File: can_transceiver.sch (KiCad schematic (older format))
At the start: 9 parts

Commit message: Add vias and ground connections
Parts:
- gave numbers to parts that had none: 9
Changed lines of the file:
@@
 $EndDescr
 $Comp
-L SN65HVD256 U?
+L SN65HVD256 U201
 U 1 1 5A128E97
 P 6320 3680
-F 0 "U?" H 6320 3680 60  0000 C CNN
+F 0 "U201" H 6320 3680 60  0000 C CNN
 F 1 "SN65HVD256" H 6320 4080 60  0000 C CNN
 F 2 "breakout:TI_SOIC8" H 6320 3680 60  0001 C CNN
@@
 $EndComp
 $Comp
-L R_Small R?
+L R_Small R202
 U 1 1 5A128E9E
 P 4930 3920
-F 0 "R?" H 4960 3940 50  0000 L CNN
+F 0 "R202" H 4960 3940 50  0000 L CNN
 F 1 "10k" H 4960 3880 50  0000 L CNN
 F 2 "Resistors_SMD:R_0805_HandSoldering" H 4930 3920 50  0001 C CNN
@@
 $EndComp
 $Comp
-L GND #PWR?
+L GND #PWR01
 U 1 1 5A128EA5
 P 6170 4310
-F 0 "#PWR?" H 6170 4060 50  0001 C CNN
+F 0 "#PWR01" H 6170 4060 50  0001 C CNN
 F 1 "GND" H 6170 4160 50  0000 C CNN
 F 2 "" H 6170 4310 50  0001 C CNN
@@
 $EndComp
 $Comp
-L C_Small C?
+L C_Small C201
 U 1 1 5A128EAB
 P 4800 3360
-F 0 "C?" H 4810 3430 50  0000 L CNN
+F 0 "C201" H 4810 3430 50  0000 L CNN
 F 1 "0u1" H 4810 3280 50  0000 L CNN
 F 2 "Capacitors_SMD:C_0805_HandSoldering" H 4800 3360 50  0001 C CNN
@@
 $EndComp
 $Comp
-L GND #PWR?
+L GND #PWR02
 U 1 1 5A128EB2
 P 4800 4100
-F 0 "#PWR?" H 4800 3850 50  0001 C CNN
+F 0 "#PWR02" H 4800 3850 50  0001 C CNN
 F 1 "GND" H 4800 3950 50  0000 C CNN
 F 2 "" H 4800 4100 50  0001 C CNN
@@
 $EndComp
 $Comp
-L Conn_01x05 J?
+L Conn_01x05 J202
 U 1 1 5A128EB8
 P 4070 3680
-F 0 "J?" H 4070 3980 50  0000 C CNN
+F 0 "J202" H 4070 3980 50  0000 C CNN
 F 1 "Conn_01x05" H 4070 3380 50  0000 C CNN
 F 2 "breakout:M20-7890546" H 4070 3680 50  0001 C CNN
@@
 $EndComp
 $Comp
-L GND #PWR?
+L GND #PWR03
 U 1 1 5A128EBF
 P 4360 3940
-F 0 "#PWR?" H 4360 3690 50  0001 C CNN
+F 0 "#PWR03" H 4360 3690 50  0001 C CNN
 F 1 "GND" H 4360 3790 50  0000 C CNN
 F 2 "" H 4360 3940 50  0001 C CNN
@@
 $EndComp
 $Comp
-L R_Small R?
+L R_Small R201
 U 1 1 5A128EC5
 P 7360 3860
-F 0 "R?" H 7390 3880 50  0000 L CNN
+F 0 "R201" H 7390 3880 50  0000 L CNN
 F 1 "60" H 7390 3820 50  0000 L CNN
 F 2 "Resistors_SMD:R_1206_HandSoldering" H 7360 3860 50  0001 C CNN
@@
 $EndComp
 $Comp
-L R_Small R?
+L R_Small R203
 U 1 1 5A128ECC
 P 7360 4130
-F 0 "R?" H 7390 4150 50  0000 L CNN
+F 0 "R203" H 7390 4150 50  0000 L CNN
 F 1 "60" H 7390 4090 50  0000 L CNN
 F 2 "Resistors_SMD:R_1206_HandSoldering" H 7360 4130 50  0001 C CNN
@@
 $EndComp
 $Comp
-L GND #PWR?
+L GND #PWR04
 U 1 1 5A128ED3
 P 7600 4370
-F 0 "#PWR?" H 7600 4120 50  0001 C CNN
+F 0 "#PWR04" H 7600 4120 50  0001 C CNN
 F 1 "GND" H 7600 4220 50  0000 C CNN
 F 2 "" H 7600 4370 50  0001 C CNN
@@
 $EndComp
 $Comp
-L C_Small C?
+L C_Small C202
 U 1 1 5A128ED9
 P 7600 4130
-F 0 "C?" H 7610 4200 50  0000 L CNN
+F 0 "C202" H 7610 4200 50  0000 L CNN
 F 1 "10n" H 7610 4050 50  0000 L CNN
 F 2 "Capacitors_SMD:C_0805_HandSoldering" H 7600 4130 50  0001 C CNN
@@
 $EndComp
 $Comp
-L GND #PWR?
+L GND #PWR05
 U 1 1 5A128EE0
 P 7690 3380
-F 0 "#PWR?" H 7690 3130 50  0001 C CNN
+F 0 "#PWR05" H 7690 3130 50  0001 C CNN
 F 1 "GND" H 7690 3230 50  0000 C CNN
 F 2 "" H 7690 3380 50  0001 C CNN
@@
 $EndComp
 $Comp
-L Screw_Terminal_01x02 J?
+L Screw_Terminal_01x02 J203
 U 1 1 5A128EE6
 P 8350 3680
-F 0 "J?" H 8350 3780 50  0000 C CNN
+F 0 "J203" H 8350 3780 50  0000 C CNN
 F 1 "Screw_Terminal_01x02" H 8350 3480 50  0000 C CNN
 F 2 "breakout:1729128" H 8350 3680 50  0001 C CNN
@@
 $EndComp
 $Comp
-L Screw_Terminal_01x02 J?
+L Screw_Terminal_01x02 J201
 U 1 1 5A128EED
 P 8000 3180
-F 0 "J?" H 8000 3280 50  0000 C CNN
+F 0 "J201" H 8000 3280 50  0000 C CNN
 F 1 "Screw_Terminal_01x02" H 8000 2980 50  0000 C CNN
 F 2 "breakout:1729128" H 8000 3180 50  0001 C CNN

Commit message: Add hierarchial pins for CAN, TODO regen netlist
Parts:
- added R204: DNC, Resistors_SMD:R_0805_HandSoldering, symbol R_Small
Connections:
- net at C201.1, J202.5 (Pin_5), U201.5 (VRXD): now also R204.1
- net at J202.4 (Pin_4), R202.1, U201.8 (S): now also R204.2
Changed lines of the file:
@@
 $EndComp
 $Comp
-L GND #PWR01
+L GND #PWR204
 U 1 1 5A128EA5
 P 6170 4310
-F 0 "#PWR01" H 6170 4060 50  0001 C CNN
+F 0 "#PWR204" H 6170 4060 50  0001 C CNN
 F 1 "GND" H 6170 4160 50  0000 C CNN
 F 2 "" H 6170 4310 50  0001 C CNN
@@
 $EndComp
 $Comp
-L GND #PWR02
+L GND #PWR203
 U 1 1 5A128EB2
 P 4800 4100
-F 0 "#PWR02" H 4800 3850 50  0001 C CNN
+F 0 "#PWR203" H 4800 3850 50  0001 C CNN
 F 1 "GND" H 4800 3950 50  0000 C CNN
 F 2 "" H 4800 4100 50  0001 C CNN
@@
 $EndComp
 $Comp
-L GND #PWR03
+L GND #PWR202
 U 1 1 5A128EBF
 P 4360 3940
-F 0 "#PWR03" H 4360 3690 50  0001 C CNN
+F 0 "#PWR202" H 4360 3690 50  0001 C CNN
 F 1 "GND" H 4360 3790 50  0000 C CNN
 F 2 "" H 4360 3940 50  0001 C CNN
@@
 $EndComp
 $Comp
-L GND #PWR04
+L GND #PWR205
 U 1 1 5A128ED3
 P 7600 4370
-F 0 "#PWR04" H 7600 4120 50  0001 C CNN
+F 0 "#PWR205" H 7600 4120 50  0001 C CNN
 F 1 "GND" H 7600 4220 50  0000 C CNN
 F 2 "" H 7600 4370 50  0001 C CNN
@@
 $EndComp
 $Comp
-L GND #PWR05
+L GND #PWR201
 U 1 1 5A128EE0
 P 7690 3380
-F 0 "#PWR05" H 7690 3130 50  0001 C CNN
+F 0 "#PWR201" H 7690 3130 50  0001 C CNN
 F 1 "GND" H 7690 3230 50  0000 C CNN
 F 2 "" H 7690 3380 50  0001 C CNN
@@
 	4930 4080 4800 4080
 Connection ~ 4800 4080
+$Comp
+L R_Small R204
+U 1 1 5A135070
+P 5060 3390
+F 0 "R204" H 5090 3410 50  0000 L CNN
+F 1 "DNC" H 5090 3350 50  0000 L CNN
+F 2 "Resistors_SMD:R_0805_HandSoldering" H 5060 3390 50  0001 C CNN
+F 3 "" H 5060 3390 50  0001 C CNN
+	1    5060 3390
+	1    0    0    -1
+$EndComp
+Wire Wire Line
+	5060 3490 5060 3580
+Connection ~ 5060 3580
+Wire Wire Line
+	5060 3290 5060 3180
+Connection ~ 5060 3180
 $EndSCHEMATC

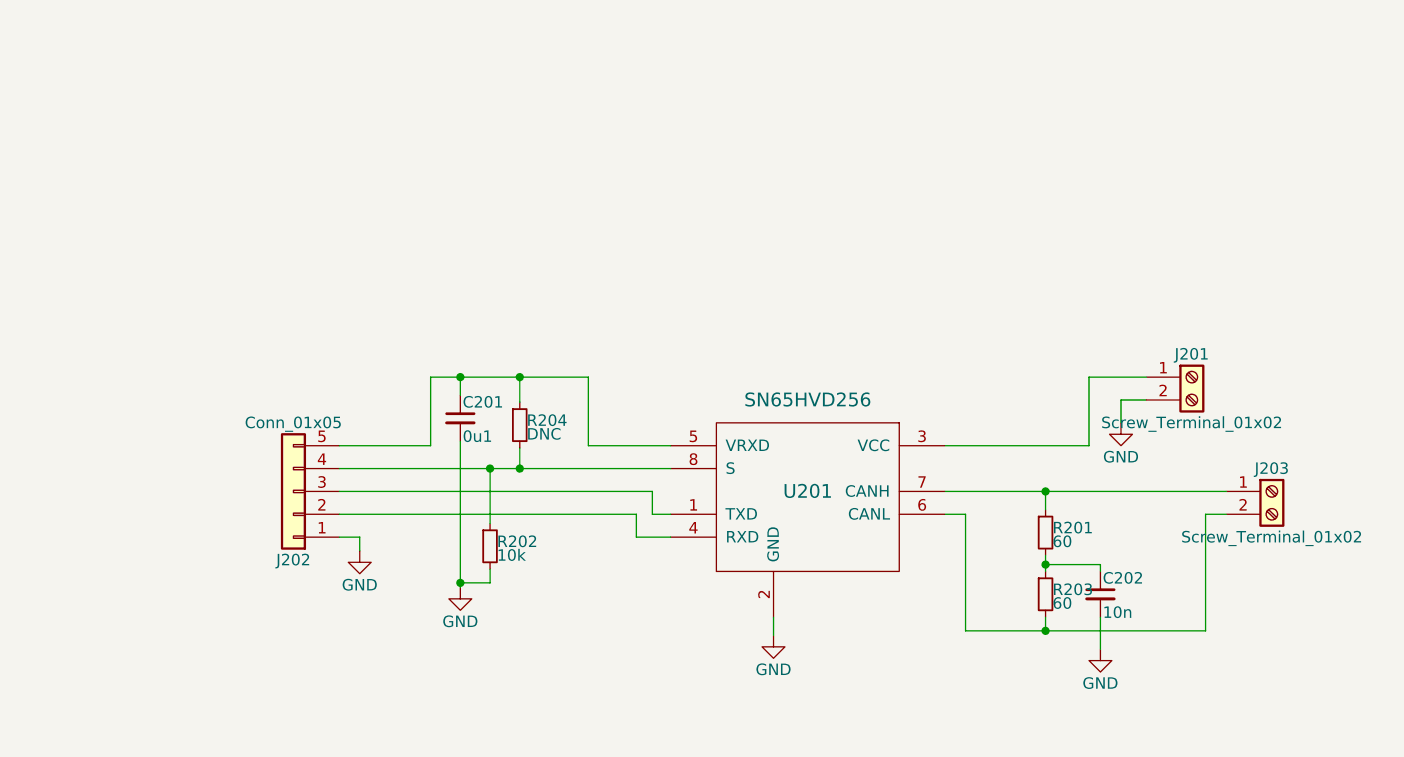
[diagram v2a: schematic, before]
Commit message: Add some protection diodes, connect most things up TODO add TVS diodes to CAN bus terinals
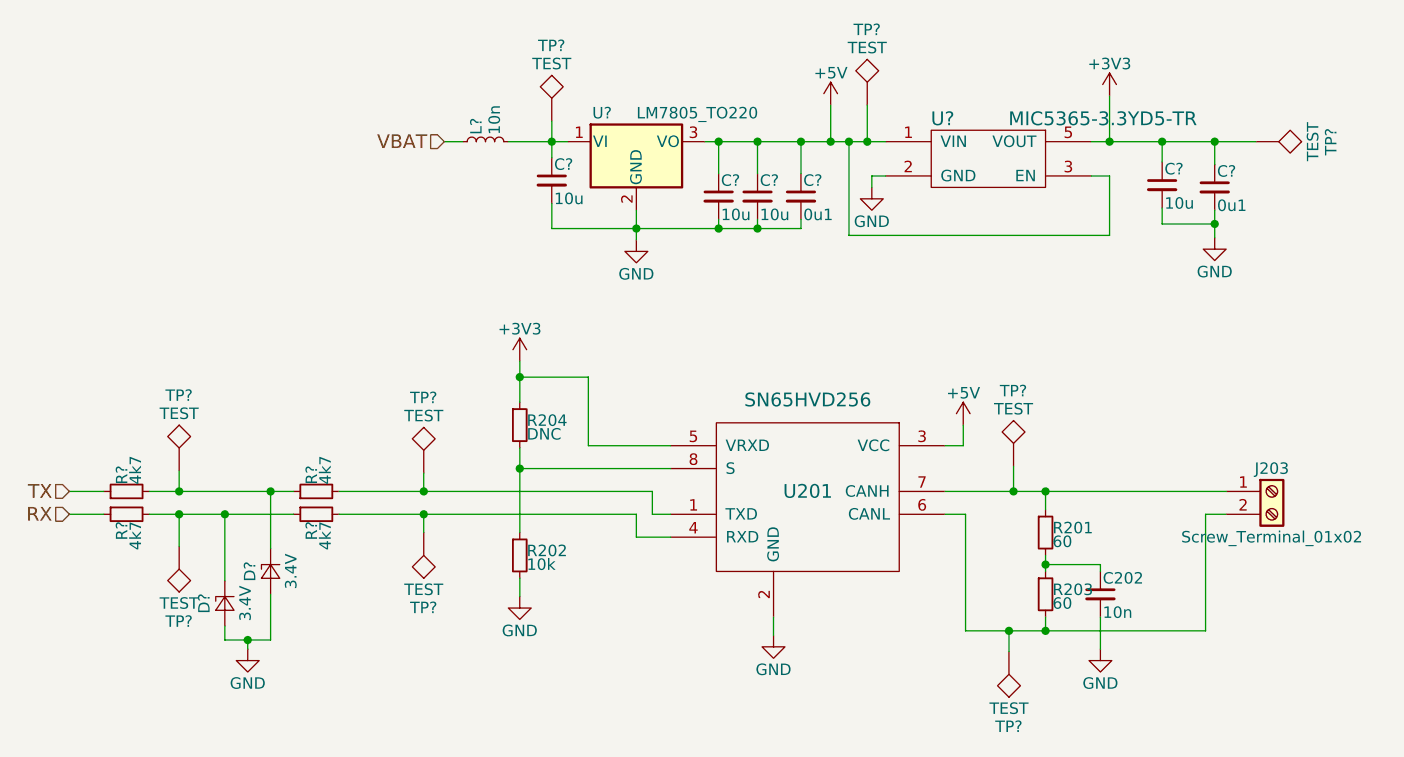
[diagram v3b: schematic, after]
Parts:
- removed C201: 0u1, Capacitors_SMD:C_0805_HandSoldering, symbol C_Small
- removed J201: Screw_Terminal_01x02, breakout:1729128, symbol Screw_Terminal_01x02
- removed J202: Conn_01x05, breakout:M20-7890546, symbol Conn_01x05
- added C? (x4): 10u, symbol C_Small
- added C? (x2): 0u1, symbol C_Small
- added D? (x2): 3.4V, symbol D_Zener_Small
- added L?: 10n, symbol L_Small
- added R? (x4): 4k7, symbol R_Small
- added TP? (x9): TEST, symbol TEST
- added U?: LM7805_TO220, TO_SOT_Packages_THT:TO-220_Vertical, symbol LM7805_TO220
- added U?: MIC5365-3.3YD5-TR, symbol MIC5365-3.3YD5-TR
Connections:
- net GND: now also C?.2, C?.2, C?.2, C?.2, C?.2, C?.2, D?.2 (A), D?.2 (A), U?.2 (GND), U?.2 (GND)
- net at U201.1 (TXD): now also R?.2, TP?.1
- net +5V: now reaches U201.3 (VCC)
- net +5V: now also C?.1, C?.1, C?.1, TP?.1, U?.1 (VIN), U?.3 (EN), U?.3 (VO)
- net at U201.4 (RXD): now also R?.2, TP?.1
- net +3V3: now reaches R204.1, U201.5 (VRXD)
- net +3V3: now also C?.1, C?.1, TP?.1, U?.5 (VOUT)
- net at J203.2 (Pin_2), R203.2, U201.6 (CANL): now also TP?.1
- net at J203.1 (Pin_1), R201.1, U201.7 (CANH): now also TP?.1
- new net: D?.1 (K), R?.1, R?.2, TP?.1 (x2)
- new net: C?.1, L?.2, TP?.1, U?.1 (VI)
- new net RX: R?.1
- new net TX: R?.1
- new net VBAT: L?.1
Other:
- moved on the sheet: R202

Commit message: Module outline added to PCB, first CAN bus added
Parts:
- removed D? (x2): 3.4V, symbol D_Zener_Small
- removed R? (x2): 4k7, symbol R_Small
- added TP210: TEST, Measurement_Points:Measurement_Point_Round-SMD-Pad_Big, symbol TEST
- C201, C203, C204, C205, C206, C207: renamed from C?; footprint (none) -> Capacitors_SMD:C_1206_HandSoldering
- J203: footprint breakout:1729128 -> breakout:39532-0002
- L201: renamed from L?; value 10n -> Ferrite; footprint (none) -> Resistors_SMD:R_1206_HandSoldering
- R206, R208: renamed from R?; footprint (none) -> Resistors_SMD:R_1206_HandSoldering
- TP201, TP202, TP203, TP204, TP205, TP206, TP207, TP208, TP209: renamed from TP?; footprint (none) -> Measurement_Points:Measurement_Point_Round-SMD-Pad_Big
- U202: renamed from U?; footprint TO_SOT_Packages_THT:TO-220_Vertical -> TO_SOT_Packages_THT:TO-220-3_Horizontal
- U203: renamed from U?; footprint (none) -> TO_SOT_Packages_SMD:SOT-23-5
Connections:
- net GND: now also TP210.1
- net RX: now also R208.1, TP208.1
- net TX: now also R206.1, TP205.1
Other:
- moved on the sheet: TP205, TP208

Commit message: Parts laid out, only routing left
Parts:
- removed C201, C205, C206: 10u, Capacitors_SMD:C_1206_HandSoldering, symbol C_Small
- removed C204, C207: 0u1, Capacitors_SMD:C_1206_HandSoldering, symbol C_Small
- removed L201: Ferrite, Resistors_SMD:R_1206_HandSoldering, symbol L_Small
- removed TP201, TP202, TP203, TP210: TEST, Measurement_Points:Measurement_Point_Round-SMD-Pad_Big, symbol TEST
- removed U202: LM7805_TO220, TO_SOT_Packages_THT:TO-220-3_Horizontal, symbol LM7805_TO220
- removed U203: MIC5365-3.3YD5-TR, TO_SOT_Packages_SMD:SOT-23-5, symbol MIC5365-3.3YD5-TR
- added C202: 0u1, Capacitors_SMD:C_1206_HandSoldering, symbol C_Small
- C203: value 10u -> 0u1
- TP201: renamed from TP204; footprint Measurement_Points:Measurement_Point_Round-SMD-Pad_Big -> Measurement_Points:Measurement_Point_Round-SMD-Pad_Small
- TP202: renamed from TP205; footprint Measurement_Points:Measurement_Point_Round-SMD-Pad_Big -> Measurement_Points:Measurement_Point_Round-SMD-Pad_Small
- TP203: renamed from TP206; footprint Measurement_Points:Measurement_Point_Round-SMD-Pad_Big -> Measurement_Points:Measurement_Point_Round-SMD-Pad_Small
- TP204: renamed from TP207; footprint Measurement_Points:Measurement_Point_Round-SMD-Pad_Big -> Measurement_Points:Measurement_Point_Round-SMD-Pad_Small
- TP205: renamed from TP208; footprint Measurement_Points:Measurement_Point_Round-SMD-Pad_Big -> Measurement_Points:Measurement_Point_Round-SMD-Pad_Small
- TP206: renamed from TP209; footprint Measurement_Points:Measurement_Point_Round-SMD-Pad_Big -> Measurement_Points:Measurement_Point_Round-SMD-Pad_Small
- renumbered C202 to C201, J203 to J201, R204 to R201, R206 to R202, R208 to R203, R201 to R204, R202 to R205, R203 to R206
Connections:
- net +5V: now also C202.1
- net GND: now also C202.2
